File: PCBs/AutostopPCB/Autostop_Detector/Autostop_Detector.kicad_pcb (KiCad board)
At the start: 2 copper layers, 52 x 100 mm, 15 parts, among them J5 DSUB9 to backplane, P1 282837-2, U1 ESP32-S3-DevKitC, U2 SN65HVD230

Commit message: Revert "added driver controls v2"
This reverts commit c73e8f860f70517a898f0b3e351800c05ab551df.
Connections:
- R1 pad 2: Net-(U1-GPIO1/ADC1_CH0) -> unconnected-(R1-Pad2)
- R2 pad 1: Net-(U1-GPIO1/ADC1_CH0) -> unconnected-(R1-Pad2)
- R3 pad 2: Net-(U1-GPIO2/ADC1_CH1) -> unconnected-(R3-Pad2)
- R5 pad 1: Net-(U1-GPIO2/ADC1_CH1) -> unconnected-(R3-Pad2)
- U1 pad 40: Net-(U1-GPIO2/ADC1_CH1) -> unconnected-(R3-Pad2)
- U1 pad 41: Net-(U1-GPIO1/ADC1_CH0) -> unconnected-(R1-Pad2)
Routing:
- net GND: track 9.35 -> 151.3 mm, vias 5 -> 6
- net unconnected-(R3-Pad2): track 0.00 -> 29.4 mm
- net Net-(U1-GPIO2/ADC1_CH1): track 29.4 -> 0.00 mm
- net unconnected-(R1-Pad2): track 0.00 -> 24.4 mm
- net Net-(U1-GPIO1/ADC1_CH0): track 24.4 -> 0.00 mm
- net /CANH: track 40.6 -> 28.1 mm
- net +3V3: track 24.7 -> 29.4 mm, vias 0 -> 2
- net /CANL: track 36.5 -> 33.9 mm
- added copper zone on In1.Cu, net GND
- removed copper zone on B.Cu, net GND
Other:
- copper layers 2 -> 4

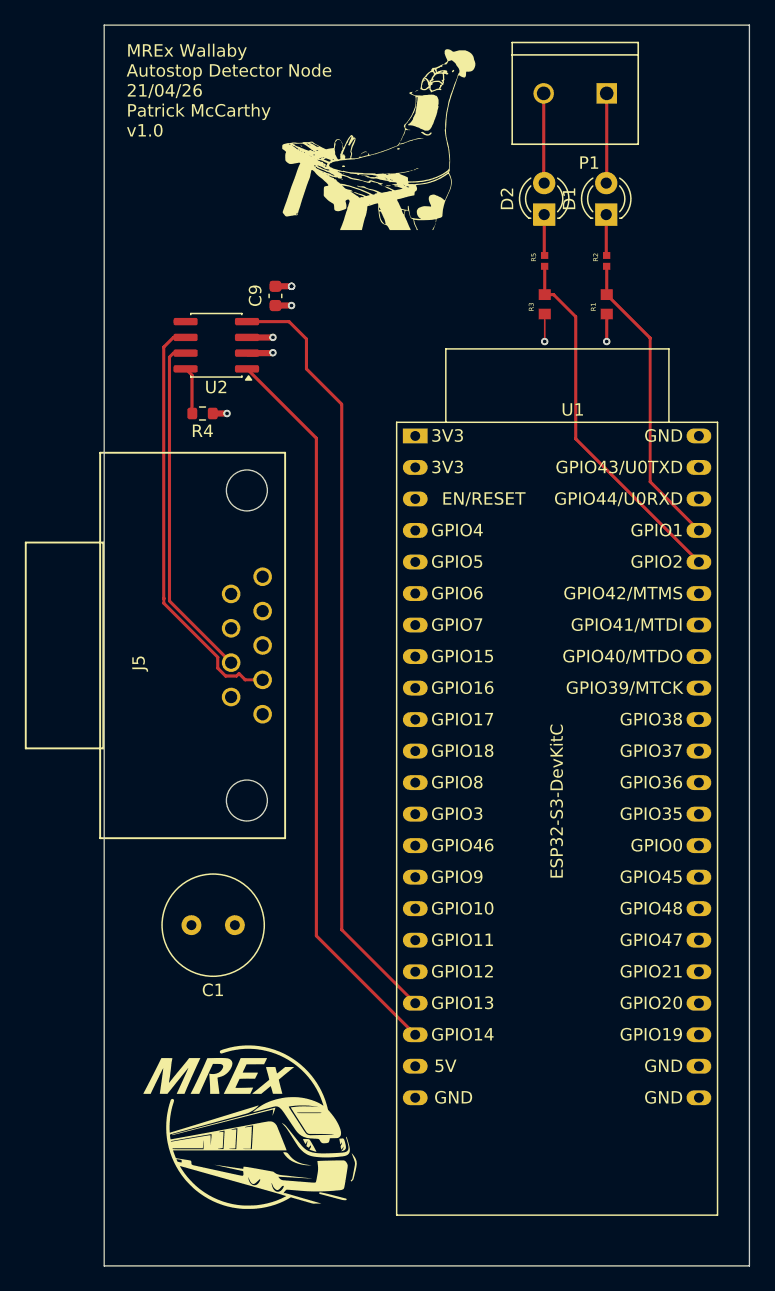
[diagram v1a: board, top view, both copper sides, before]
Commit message: Reapply "added driver controls v2"
This reverts commit d70487c3c1110107dce6cdfc2b36a156bfb5c696.
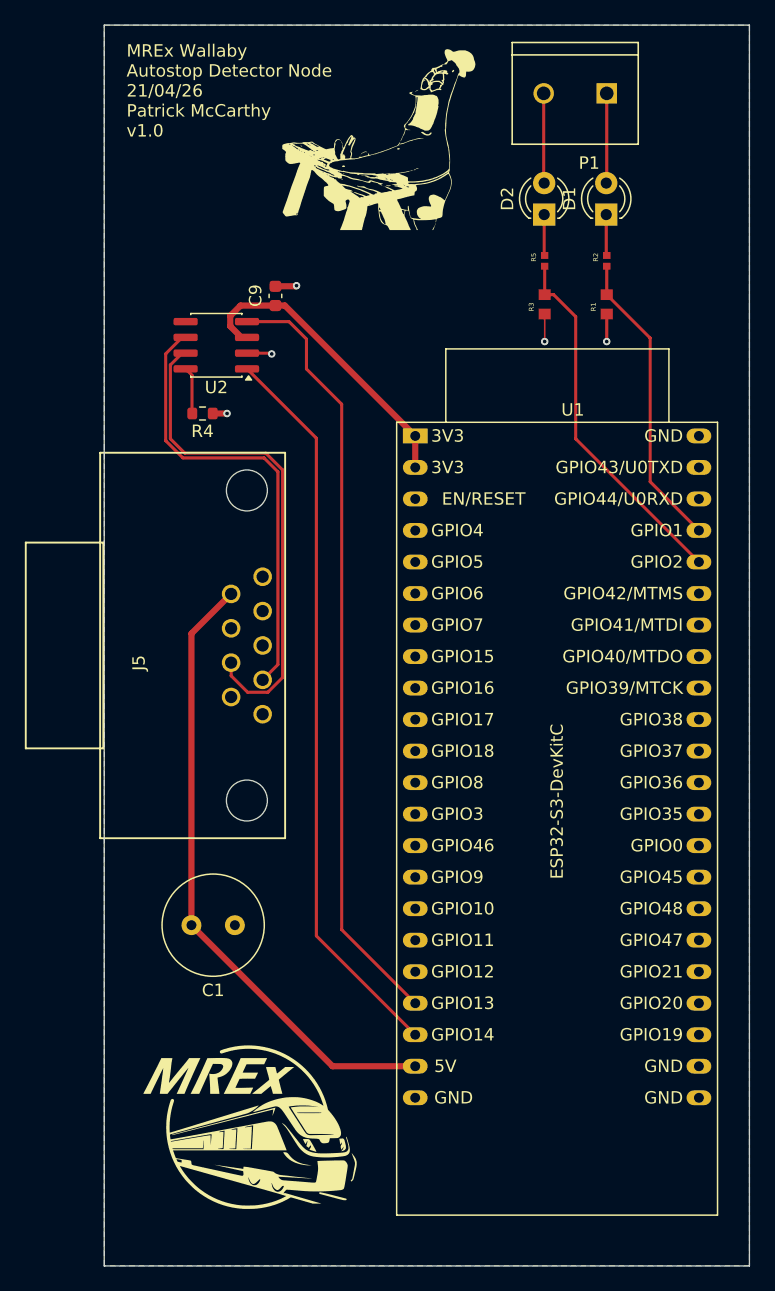
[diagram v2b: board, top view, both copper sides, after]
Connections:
- R1 pad 2: unconnected-(R1-Pad2) -> Net-(U1-GPIO1/ADC1_CH0)
- R2 pad 1: unconnected-(R1-Pad2) -> Net-(U1-GPIO1/ADC1_CH0)
- R3 pad 2: unconnected-(R3-Pad2) -> Net-(U1-GPIO2/ADC1_CH1)
- R5 pad 1: unconnected-(R3-Pad2) -> Net-(U1-GPIO2/ADC1_CH1)
- U1 pad 40: unconnected-(R3-Pad2) -> Net-(U1-GPIO2/ADC1_CH1)
- U1 pad 41: unconnected-(R1-Pad2) -> Net-(U1-GPIO1/ADC1_CH0)
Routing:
- net GND: track 151.3 -> 9.35 mm, vias 6 -> 5
- net unconnected-(R3-Pad2): track 29.4 -> 0.00 mm
- net Net-(U1-GPIO2/ADC1_CH1): track 0.00 -> 29.4 mm
- net unconnected-(R1-Pad2): track 24.4 -> 0.00 mm
- net Net-(U1-GPIO1/ADC1_CH0): track 0.00 -> 24.4 mm
- net /CANH: track 28.1 -> 40.6 mm
- net +3V3: track 29.4 -> 24.7 mm, vias 2 -> 0
- net /CANL: track 33.9 -> 36.5 mm
- added copper zone on B.Cu, net GND
- removed copper zone on In1.Cu, net GND
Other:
- copper layers 4 -> 2
